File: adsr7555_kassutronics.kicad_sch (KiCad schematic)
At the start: 0 parts

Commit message: SCH v1 needs QC against web schematic
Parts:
- added C2: 10n, Capacitor_THT:C_Disc_D10.0mm_W2.5mm_P5.00mm, symbol Device:C
- added C4, C5: C_Polarized_US, Capacitor_THT:CP_Radial_D12.5mm_P5.00mm, symbol Device:C_Polarized_US
- added C6, C7: 1n, Capacitor_THT:C_Disc_D10.0mm_W2.5mm_P5.00mm, symbol Device:C
- added C8: 1u Tant, Capacitor_THT:CP_Radial_D12.5mm_P5.00mm, symbol Device:C_Polarized_US
- added D1, D2, D3, D4, D5: 1N4148, Diode_THT:D_DO-35_SOD27_P7.62mm_Horizontal, symbol Diode:1N4148
- added D6: LED, symbol Device:LED
- added J1: Power, Connector_Molex:Molex_KK-254_AE-6410-03A_1x03_P2.54mm_Vertical, symbol Connector_Generic:Conn_01x03
- added J2: GateIn, Connector_Molex:Molex_KK-254_AE-6410-02A_1x02_P2.54mm_Vertical, symbol Connector_Generic:Conn_01x02
- added J3: Trigger, Connector_Molex:Molex_KK-254_AE-6410-02A_1x02_P2.54mm_Vertical, symbol Connector_Generic:Conn_01x02
- added J4: Gate, Connector_Molex:Molex_KK-254_AE-6410-02A_1x02_P2.54mm_Vertical, symbol Connector_Generic:Conn_01x02
- added J5: Atten Out, Connector_Molex:Molex_KK-254_AE-6410-02A_1x02_P2.54mm_Vertical, symbol Connector_Generic:Conn_01x02
- added J6: Output, Connector_Molex:Molex_KK-254_AE-6410-02A_1x02_P2.54mm_Vertical, symbol Connector_Generic:Conn_01x02
- added Q1, Q2, Q3, Q4: NPN, Package_TO_SOT_THT:TO-92_Inline_Wide, symbol Simulation_SPICE:NPN
- added R1, R2, R20: 10k, Resistor_THT:R_Axial_DIN0204_L3.6mm_D1.6mm_P7.62mm_Horizontal, symbol Device:R_US
- added R10, R12, R8: 100, Resistor_THT:R_Axial_DIN0204_L3.6mm_D1.6mm_P7.62mm_Horizontal, symbol Device:R_US
- added R15, R3, R4, R6, R7: 4k7, Resistor_THT:R_Axial_DIN0204_L3.6mm_D1.6mm_P7.62mm_Horizontal, symbol Device:R_US
- added R17, R18: 100k, Resistor_THT:R_Axial_DIN0204_L3.6mm_D1.6mm_P7.62mm_Horizontal, symbol Device:R_US
- added R19, R22: 1k, Resistor_THT:R_Axial_DIN0204_L3.6mm_D1.6mm_P7.62mm_Horizontal, symbol Device:R_US
- added R21: 47k, Resistor_THT:R_Axial_DIN0204_L3.6mm_D1.6mm_P7.62mm_Horizontal, symbol Device:R_US
- added R5: 22k, Resistor_THT:R_Axial_DIN0204_L3.6mm_D1.6mm_P7.62mm_Horizontal, symbol Device:R_US
- added R9: 33k, Resistor_THT:R_Axial_DIN0204_L3.6mm_D1.6mm_P7.62mm_Horizontal, symbol Device:R_US
- added RV11: 1M Log Release, Connector_Molex:Molex_KK-254_AE-6410-03A_1x03_P2.54mm_Vertical, symbol Device:R_Potentiometer_US
- added RV13: 1M Log Decay, Connector_Molex:Molex_KK-254_AE-6410-03A_1x03_P2.54mm_Vertical, symbol Device:R_Potentiometer_US
- added RV14: 10K Lin, Connector_Molex:Molex_KK-254_AE-6410-03A_1x03_P2.54mm_Vertical, symbol Device:R_Potentiometer_US
- added RV15: 100k Lin Atten, Connector_Molex:Molex_KK-254_AE-6410-03A_1x03_P2.54mm_Vertical, symbol Device:R_Potentiometer_US
- added RV9: 1M Log, Connector_Molex:Molex_KK-254_AE-6410-03A_1x03_P2.54mm_Vertical, symbol Device:R_Potentiometer_US
- added SW1: SW_Push, symbol Switch:SW_Push
- added U1: ICM7555xP, Package_DIP:DIP-8_W7.62mm, symbol Timer:ICM7555xP
- added U2: TL074, symbol Amplifier_Operational:TL074
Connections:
- new net: D5.2 (A), U1.3 (OUT)
- new net: C2.1, U1.5 (CONT)
- new net: R17.1, RV15.3, U1.6 (THRES), U2.9 (-)
- new net: RV14.3, U1.7 (DISCH)
- new net: RV15.2, U2.5 (+)
- new net: D6.1 (K), Q4.1 (C)
- new net: Q4.2 (B), R9.1
- new net: R10.2, RV11.1, RV11.2
- new net: C8.1, RV11.3, RV13.3, RV9.3, U2.10 (+)
- new net: R22.2, R9.2, U2.8
- new net: R20.1, SW1.2
- new net: D3.1 (K), U2.1
- new net: D3.2 (A), R10.1, U2.2 (-)
- new net: Q1.1 (C), R3.1, R5.2
- new net: C7.2, D2.1 (K), R1.1
- new net: D1.1 (K), Q1.2 (B), R2.2, R21.2
- new net: R21.1, SW1.1
- new net: RV14.2, U2.12 (+)
- new net: D4.2 (A), R12.1, U2.13 (-)
- new net: D4.1 (K), U2.14
- new net: Q3.1 (C), R6.1
- new net: Q2.2 (B), R5.1
- new net: R17.2, R18.2, U2.6 (-)
- new net: J2.1 (Pin_1), R2.1
- new net: D5.1 (K), R8.1
- new net: Q3.2 (B), R1.2
- new net: R12.2, RV13.1, RV13.2
- new net: R8.2, RV9.1, RV9.2
- new net: R18.1, R19.2, U2.7
- new net: D6.2 (A), R7.1
- new net: R15.1, RV14.1
- new net +15V: C5.1, C6.1, J1.1 (Pin_1), J3.1 (Pin_1), R15.2, R20.2, R3.2, R4.2, R6.2, R7.2, U1.2 (TRIG), U1.8 (VCC), U2.4 (V+)
- new net -15V: C4.2, C6.2, J1.3 (Pin_3), U2.11 (V-)
- new net ATTENOUT: J5.1 (Pin_1), R19.1
- new net GATE: C7.1, J4.1 (Pin_1), Q2.1 (C), R4.1, U1.4 (~{RST}), U2.3 (+)
- new net GND: C2.2, C4.1, C5.2, C8.2, D1.2 (A), D2.2 (A), J1.2 (Pin_2), J2.2 (Pin_2), J3.2 (Pin_2), J4.2 (Pin_2), J5.2 (Pin_2), J6.2 (Pin_2), Q1.3 (E), Q2.3 (E), Q3.3 (E), Q4.3 (E), RV15.1, U1.1 (GND)
- new net OUTPUT: J6.1 (Pin_1), R22.1
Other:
- note added: "ccw"
- note added: "cw"
- company: (none) -> John Ellinger
- title: (none) -> Kassutronics Precision ADSR

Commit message: PCB layout in progress
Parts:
- removed R6: 4k7, Resistor_THT:R_Axial_DIN0204_L3.6mm_D1.6mm_P7.62mm_Horizontal, symbol Device:R_US
- added C9: 1n, Capacitor_THT:C_Disc_D10.0mm_W2.5mm_P5.00mm, symbol Device:C
- added R7: 4k7, Resistor_THT:R_Axial_DIN0204_L3.6mm_D1.6mm_P7.62mm_Horizontal, symbol Device:R_US
- C3: renamed from C8; footprint Capacitor_THT:CP_Radial_D12.5mm_P5.00mm -> Capacitor_THT:CP_Radial_D4.0mm_P2.00mm
- C4, C5: footprint Capacitor_THT:CP_Radial_D12.5mm_P5.00mm -> Capacitor_THT:CP_Radial_D4.0mm_P2.00mm
- D6, SW1: footprint (none) -> Connector_Molex:Molex_KK-254_AE-6410-02A_1x02_P2.54mm_Vertical
- Q1, Q2, Q3, Q4: footprint Package_TO_SOT_THT:TO-92_Inline_Wide -> Package_TO_SOT_THT:TO-92L_Inline_Wide
- RV14: value 10K Lin -> 10K Lin Sustain
- RV9: value 1M Log -> 1M Log Attack
- U2: footprint (none) -> Package_DIP:DIP-14_W7.62mm_Socket
- renumbered C7 to C1, R22 to R16, R7 to R6
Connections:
- net +15V: now also J1.3 (Pin_3), R7.2; no longer C6.1, J1.1 (Pin_1)
- net -15V: now also J1.1 (Pin_1); no longer C6.2, J1.3 (Pin_3)
- net GND: now also C6.2, C9.2; no longer C4.1, C5.2
- net at Q3.1 (C): now also R7.1
- new net: C5.2, C6.1
- new net: C4.1, C9.1
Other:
- moved on the sheet: C4, C5, C6, J1

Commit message: PCB Wiring complete. Need to fix silkscreen overlaps
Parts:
- C1, C2, C6: footprint Capacitor_THT:C_Disc_D10.0mm_W2.5mm_P5.00mm -> Capacitor_THT:C_Disc_D4.7mm_W2.5mm_P5.00mm
- C9: footprint Capacitor_THT:C_Disc_D10.0mm_W2.5mm_P5.00mm -> Capacitor_THT:C_Disc_D7.5mm_W2.5mm_P5.00mm
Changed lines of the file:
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@@
 			)
 		)
-		(property "Footprint" "Capacitor_THT:C_Disc_D10.0mm_W2.5mm_P5.00mm"
+		(property "Footprint" "Capacitor_THT:C_Disc_D4.7mm_W2.5mm_P5.00mm"
 			(at 106.68 62.5348 0)
 			(hide yes)
@@
 			)
 		)
-		(property "Footprint" "Capacitor_THT:C_Disc_D10.0mm_W2.5mm_P5.00mm"
+		(property "Footprint" "Capacitor_THT:C_Disc_D4.7mm_W2.5mm_P5.00mm"
 			(at 248.92 26.9748 0)
 			(hide yes)
@@
 			)
 		)
-		(property "Footprint" "Capacitor_THT:C_Disc_D10.0mm_W2.5mm_P5.00mm"
+		(property "Footprint" "Capacitor_THT:C_Disc_D7.5mm_W2.5mm_P5.00mm"
 			(at 248.92 58.7248 0)
 			(hide yes)
@@
 			)
 		)
-		(property "Footprint" "Capacitor_THT:C_Disc_D10.0mm_W2.5mm_P5.00mm"
+		(property "Footprint" "Capacitor_THT:C_Disc_D4.7mm_W2.5mm_P5.00mm"
 			(at 54.3052 149.86 0)
 			(hide yes)

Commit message: QA PCB passes
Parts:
- C4, C5: value C_Polarized_US -> 100u
- C9: footprint Capacitor_THT:C_Disc_D7.5mm_W2.5mm_P5.00mm -> Capacitor_THT:C_Disc_D4.7mm_W2.5mm_P5.00mm
- J5: value Atten Out -> Atn Out
- Q1, Q2, Q3, Q4: value NPN -> 3904
- RV11: value 1M Log Release -> 1M Log Rel
- RV13: value 1M Log Decay -> 1M Log Dky
- RV14: value 10K Lin Sustain -> 10K Lin Sus
- RV15: value 100k Lin Atten -> 100k Lin Atn; footprint Connector_Molex:Molex_KK-254_AE-6410-03A_1x03_P2.54mm_Vertical -> Potentiometer_THT:Potentiometer_Bourns_3296W_Vertical
- RV9: value 1M Log Attack -> 1M Log Atk
- U1: value ICM7555xP -> 7555
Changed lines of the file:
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@@
 		(fields_autoplaced yes)
 		(property "Reference" "U1"
-			(at 40.64 114.554 0)
+			(at 40.64 114.3 0)
 			(show_name no)
 			(do_not_autoplace no)
@@
 			)
 		)
-		(property "Value" "ICM7555xP"
-			(at 40.64 117.094 0)
+		(property "Value" "7555"
+			(at 40.64 116.84 0)
 			(show_name no)
 			(do_not_autoplace no)
@@
 			)
 		)
-		(property "Value" "100k Lin Atten"
+		(property "Value" "100k Lin Atn"
 			(at 205.74 121.9199 0)
 			(show_name no)
@@
 			)
 		)
-		(property "Footprint" "Connector_Molex:Molex_KK-254_AE-6410-03A_1x03_P2.54mm_Vertical"
+		(property "Footprint" "Potentiometer_THT:Potentiometer_Bourns_3296W_Vertical"
 			(at 203.2 120.65 0)
 			(hide yes)
@@
 			)
 		)
-		(property "Value" "NPN"
+		(property "Value" "3904"
 			(at 232.41 156.2099 0)
 			(show_name no)
@@
 			)
 		)
-		(property "Value" "1M Log Release"
+		(property "Value" "1M Log Rel"
 			(at 123.19 124.46 90)
 			(show_name no)
@@
 			)
 		)
-		(property "Value" "C_Polarized_US"
+		(property "Value" "100u"
 			(at 231.775 22.86 90)
 			(show_name no)
@@
 			)
 		)
-		(property "Value" "NPN"
+		(property "Value" "3904"
 			(at 71.12 64.7699 0)
 			(show_name no)
@@
 			)
 		)
-		(property "Value" "NPN"
+		(property "Value" "3904"
 			(at 92.71 64.7699 0)
 			(show_name no)
@@
 			)
 		)
-		(property "Value" "1M Log Decay"
+		(property "Value" "1M Log Dky"
 			(at 123.19 95.25 90)
 			(show_name no)
@@
 			)
 		)
-		(property "Value" "C_Polarized_US"
+		(property "Value" "100u"
 			(at 233.045 54.61 90)
 			(show_name no)
@@
 			)
 		)
-		(property "Footprint" "Capacitor_THT:C_Disc_D7.5mm_W2.5mm_P5.00mm"
+		(property "Footprint" "Capacitor_THT:C_Disc_D4.7mm_W2.5mm_P5.00mm"
 			(at 248.92 58.7248 0)
 			(hide yes)
@@
 			)
 		)
-		(property "Value" "Atten Out"
+		(property "Value" "Atn Out"
 			(at 182.372 62.23 0)
 			(show_name no)
@@
 			)
 		)
-		(property "Value" "NPN"
+		(property "Value" "3904"
 			(at 130.81 64.7699 0)
 			(show_name no)
@@
 			)
 		)
-		(property "Value" "1M Log Attack"
+		(property "Value" "1M Log Atk"
 			(at 123.19 152.4 90)
 			(show_name no)
@@
 		(in_pos_files yes)
 		(dnp no)
-		(fields_autoplaced yes)
 		(property "Reference" "RV14"
 			(at 67.31 109.2199 0)
@@
 			)
 		)
-		(property "Value" "10K Lin Sustain"
-			(at 67.31 111.7599 0)
+		(property "Value" "10K Lin Sus"
+			(at 67.31 110.998 0)
 			(show_name no)
 			(do_not_autoplace no)

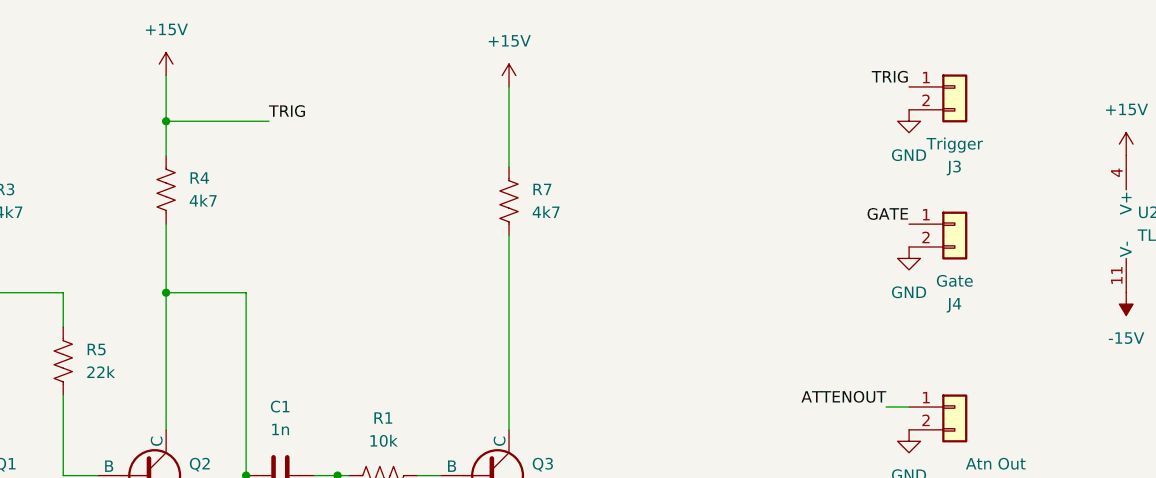
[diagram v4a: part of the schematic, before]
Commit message: removed TRIG and GATE panel connectors
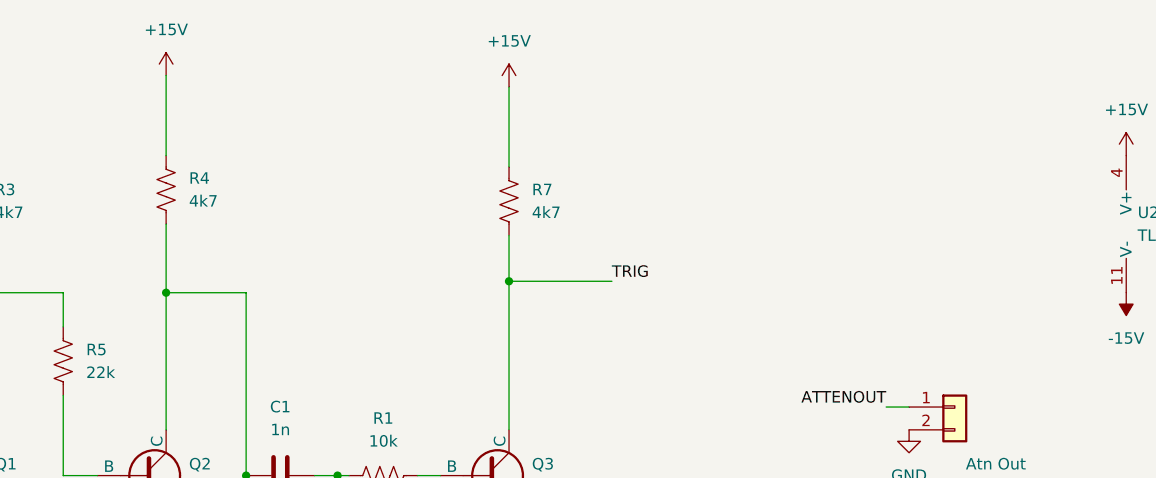
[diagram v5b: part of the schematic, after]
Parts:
- removed J3: Trigger, Connector_Molex:Molex_KK-254_AE-6410-02A_1x02_P2.54mm_Vertical, symbol Connector_Generic:Conn_01x02
- removed J4: Gate, Connector_Molex:Molex_KK-254_AE-6410-02A_1x02_P2.54mm_Vertical, symbol Connector_Generic:Conn_01x02
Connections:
- net +15V: no longer U1.2 (TRIG)
- net TRIG: now reaches Q3.1 (C), R7.1
- net TRIG: now also U1.2 (TRIG)

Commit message: update PCB wiring worked on lower right
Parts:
- C3: footprint Capacitor_THT:CP_Radial_D4.0mm_P2.00mm -> Capacitor_THT:CP_Radial_D5.0mm_P2.50mm
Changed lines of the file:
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@@
 			)
 		)
-		(property "Footprint" "Capacitor_THT:CP_Radial_D4.0mm_P2.00mm"
+		(property "Footprint" "Capacitor_THT:CP_Radial_D5.0mm_P2.50mm"
 			(at 139.7 167.64 0)
 			(hide yes)
